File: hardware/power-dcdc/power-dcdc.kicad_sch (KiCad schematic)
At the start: 69 parts, among them J1 SOLAR_IN, J2 BATT2, J3 BATT1, J4 DCDC-MEASURES, J5 DCDC-PWM, Q1 SIR164ADP, Q2 SIR164ADP, Q3 SI7149ADP, Q4 SI7149ADP, Q5 SI7149ADP, Q6 SI7149ADP, U1 LP4951C, U2 NCP5901B, U3 PAC1953-1, U4 DGD0215, U5 DGD0215

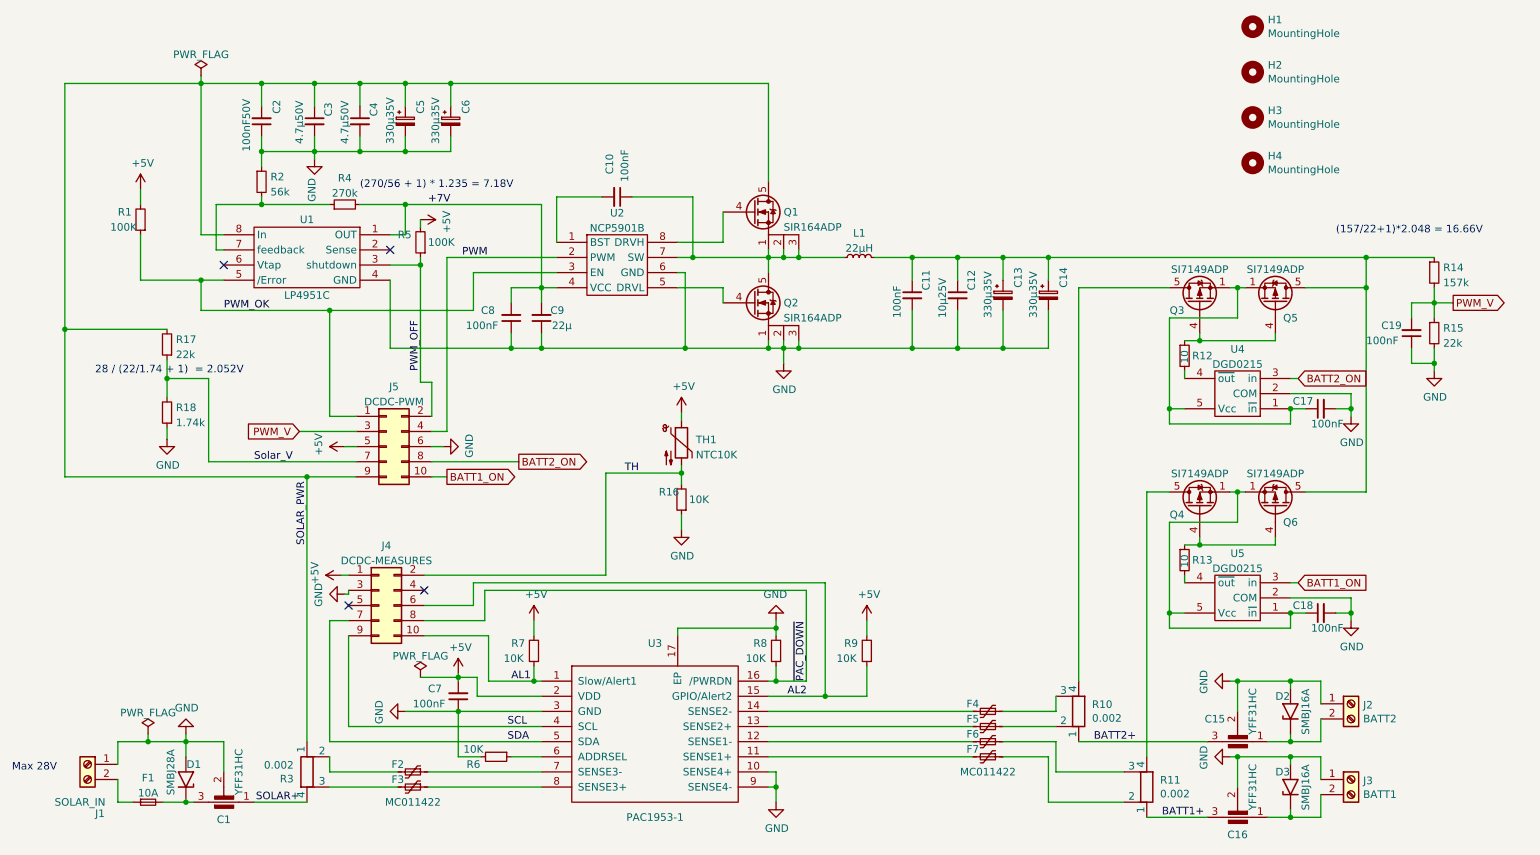
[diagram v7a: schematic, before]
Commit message: Re-annotate schematics
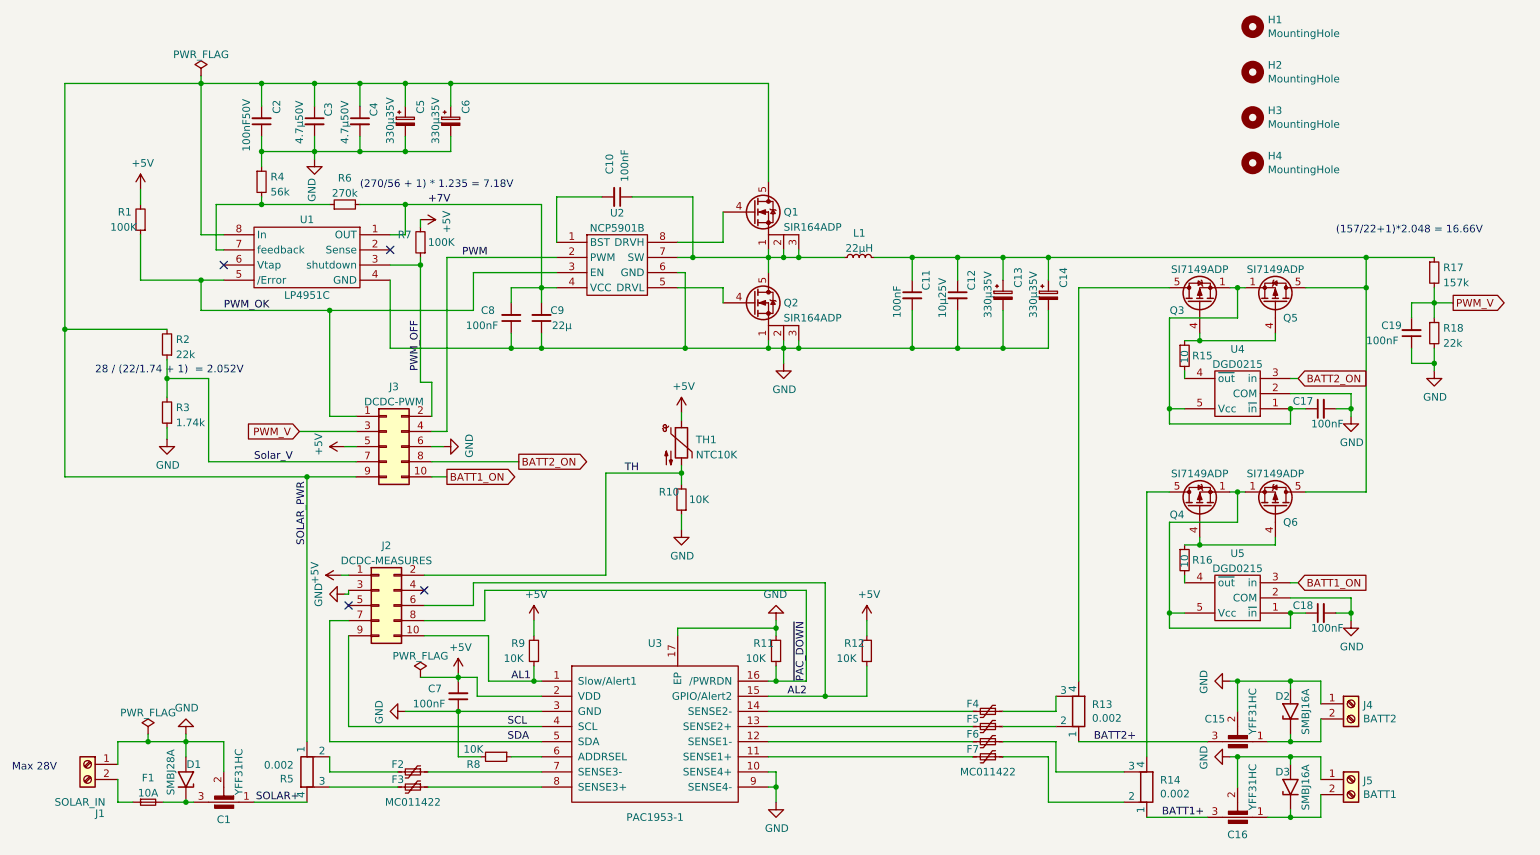
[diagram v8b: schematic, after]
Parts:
- renumbered J4 to J2, J5 to J3, J2 to J4, J3 to J5, R16 to R10, R8 to R11, R9 to R12, R10 to R13, R11 to R14, R12 to R15, R13 to R16, R14 to R17, R15 to R18, R17 to R2, R18 to R3, R2 to R4, R3 to R5, R4 to R6, R5 to R7, R6 to R8, R7 to R9
